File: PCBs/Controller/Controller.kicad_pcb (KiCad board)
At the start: 2 copper layers, 0 parts

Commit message: update sensor
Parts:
- added BZ1: Buzzer, Buzzer_Beeper:Buzzer_12x9.5RM7.6, F.Cu at (136.0, 118.7)
- added J1: RJ45, Library:WR-MJ Modular Jack Horizontal Shielded w. EMI Panel Finger 8P8C Tab Up, F.Cu at (153.0, 60.0)
- added J2: RJ45, Library:WR-MJ Modular Jack Horizontal Shielded w. EMI Panel Finger 8P8C Tab Up, F.Cu at (153.0, 80.0)
- added J3: RJ45, Library:WR-MJ Modular Jack Horizontal Shielded w. EMI Panel Finger 8P8C Tab Up, F.Cu at (153.0, 100.0)
- added J4: RJ45, Library:WR-MJ Modular Jack Horizontal Shielded w. EMI Panel Finger 8P8C Tab Up, F.Cu at (153.0, 120.0)
- added J5: Barrel_Jack_Switch, Library:WR-DC DC Power Jack Right Angled (6.4), F.Cu at (108.5, 57.2)
- added J6: Conn_01x04_Pin, Connector_PinHeader_2.54mm:PinHeader_1x04_P2.54mm_Vertical, F.Cu at (113.0, 97.0)
- added J7: Conn_01x03_Pin, Connector_PinHeader_2.54mm:PinHeader_1x03_P2.54mm_Vertical, F.Cu at (127.5, 109.5)
- added JP1: Jumper_2_Open, Jumper:SolderJumper-2_P1.3mm_Open_RoundedPad1.0x1.5mm, B.Cu at (140.0, 109.5)
- added JP2: Jumper_3_Bridged12, Jumper:SolderJumper-3_P1.3mm_Bridged12_RoundedPad1.0x1.5mm, B.Cu at (136.0, 54.0)
- added JP3: Jumper_2_Bridged, Jumper:SolderJumper-2_P1.3mm_Bridged_RoundedPad1.0x1.5mm, B.Cu at (140.0, 113.5)
- added SW1: RotaryEncoder_Switch, Library:WS-ENTV_4820XX514001, F.Cu at (110.5, 119.5)
- added SW2: SW_Push, Button_Switch_THT:SW_PUSH_6mm_H4.3mm, F.Cu at (112.5, 90.5)
- added U1: Pico, Library:RPi_Pico_SMD_TH, F.Cu at (130.1, 80.4)
- added U2: AMS1117-3.3, Package_TO_SOT_SMD:SOT-223-3_TabPin2, F.Cu at (108.5, 72.5)
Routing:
- net Net-(JP3-B): track 0.00 -> 114.1 mm, vias 0 -> 3
- net +3.3V: track 0.00 -> 113.1 mm, vias 0 -> 3
- net +5V: track 0.00 -> 108.7 mm
- net /SCL0: track 0.00 -> 95.6 mm, vias 0 -> 3
- net Net-(JP1-B): track 0.00 -> 90.3 mm, vias 0 -> 3
- net /RUN: track 0.00 -> 87.6 mm
- net /SDA0: track 0.00 -> 86.2 mm, vias 0 -> 4
- net Net-(JP2-A): track 0.00 -> 48.8 mm, vias 0 -> 1
- net /RE_S: track 0.00 -> 42.1 mm
- net /RE_A: track 0.00 -> 38.5 mm
- net /BZ1: track 0.00 -> 31.1 mm
- net /RE_B: track 0.00 -> 26.5 mm
- net /AT_RS: track 0.00 -> 18.6 mm
- net /FU: track 0.00 -> 17.3 mm
- net +3V3: track 0.00 -> 13.4 mm
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- added copper zone on F.Cu, net GND
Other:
- board outline added: 60 x 80 mm
- board text added: "Rotating Knob Radius"

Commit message: added text
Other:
- board text added: "Laser-Parkour Controller Rev. 01 © 2024 Manuel König HHN HTWG x42.space"
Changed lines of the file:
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@@
 		(layer "Edge.Cuts")
+	)
+	(gr_text "Laser-Parkour Controller Rev. 01\n© 2024 Manuel König HHN HTWG\nx42.space "
+		(at 133.81 62.5 90)
+		(layer "B.SilkS")
+		(effects
+			(font
+				(size 1.5 1.5)
+				(thickness 0.3)
+				(bold yes)
+			)
+			(justify left bottom mirror)
+		)
 	)
 	(gr_text "Rotating Knob Radius"

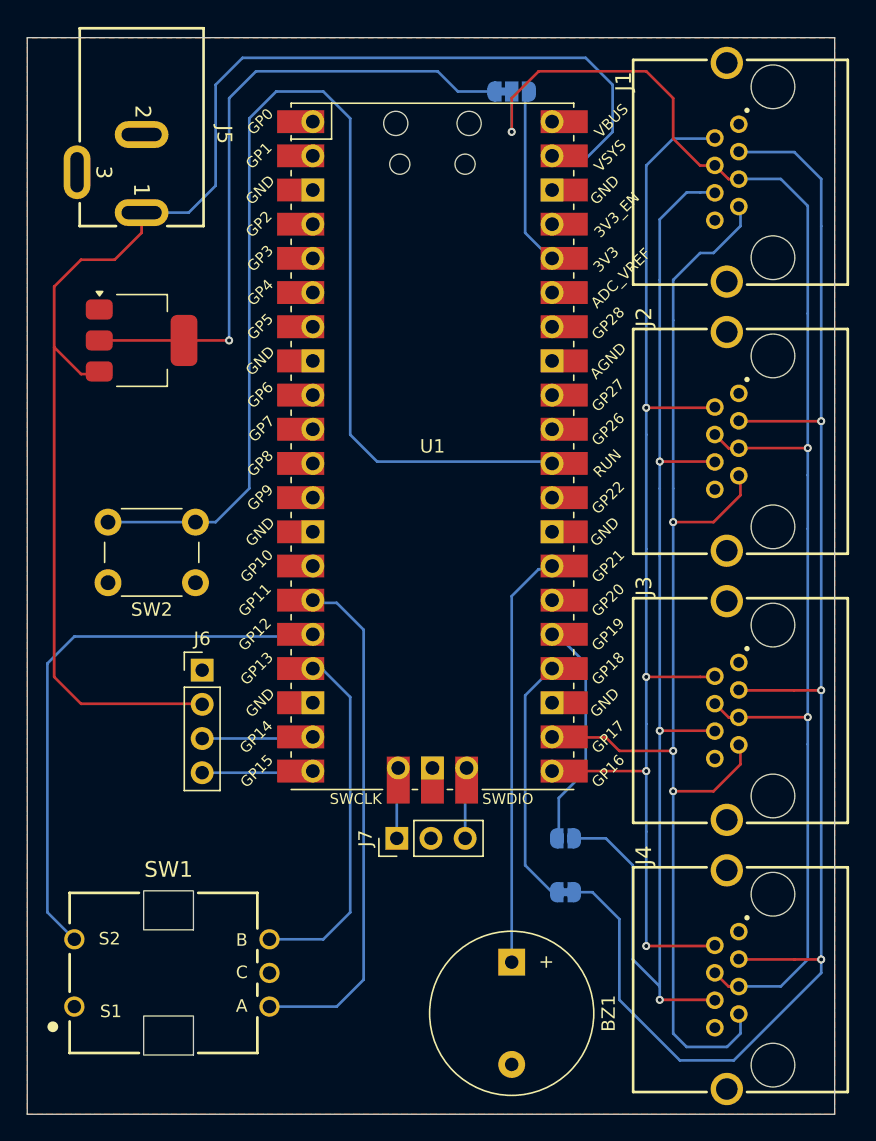
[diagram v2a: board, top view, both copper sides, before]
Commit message: added Capacitors
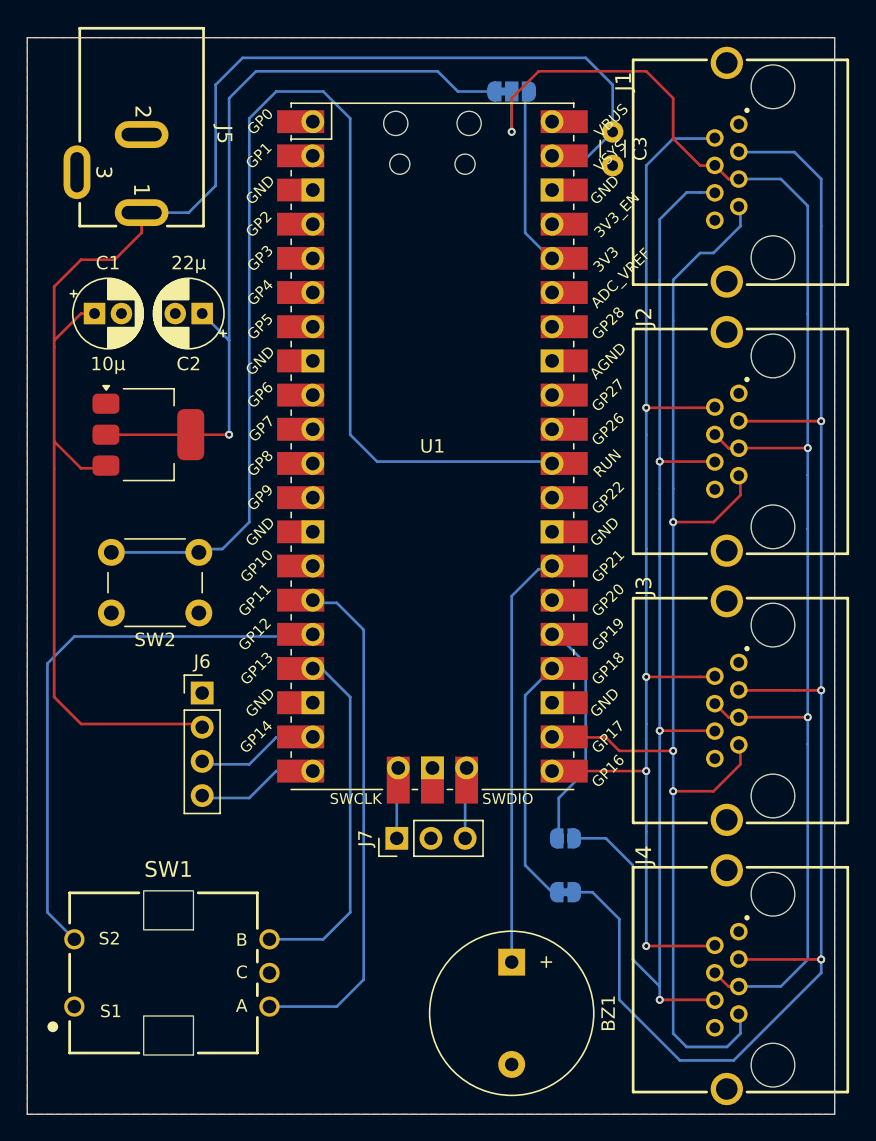
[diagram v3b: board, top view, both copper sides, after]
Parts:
- added C1: 10μ, Capacitor_THT:CP_Radial_D5.0mm_P2.00mm, F.Cu at (105.0, 70.5)
- added C2: 22μ, Capacitor_THT:CP_Radial_D5.0mm_P2.00mm, F.Cu at (113.0, 70.5)
- added C3: 0.1μ, Capacitor_THT:C_Disc_D3.0mm_W1.6mm_P2.50mm, F.Cu at (143.5, 57.0)
- moved U2 7.02 mm to (109.0, 79.5)
- moved SW2 2.26 mm to (112.8, 92.8)
- moved J6 1.70 mm to (113.0, 98.7)
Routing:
- net Net-(JP2-A): track 48.8 -> 58.1 mm
- net +5V: track 108.7 -> 114.6 mm
- net /RUN: track 87.6 -> 89.7 mm
- net /SDA1: track 8.27 -> 9.16 mm
- net /SCL1: track 8.27 -> 9.12 mm
